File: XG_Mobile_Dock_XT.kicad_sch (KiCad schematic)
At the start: 45 parts, among them J1 5-1775443-8, J13 39301240, J14 I2C1, J2 20455-040E-76, J3 20455-040E-76, J5 USB_C_Receptacle, J6 455860005, J7 10147430-113T0LF, SW1 SW_Push

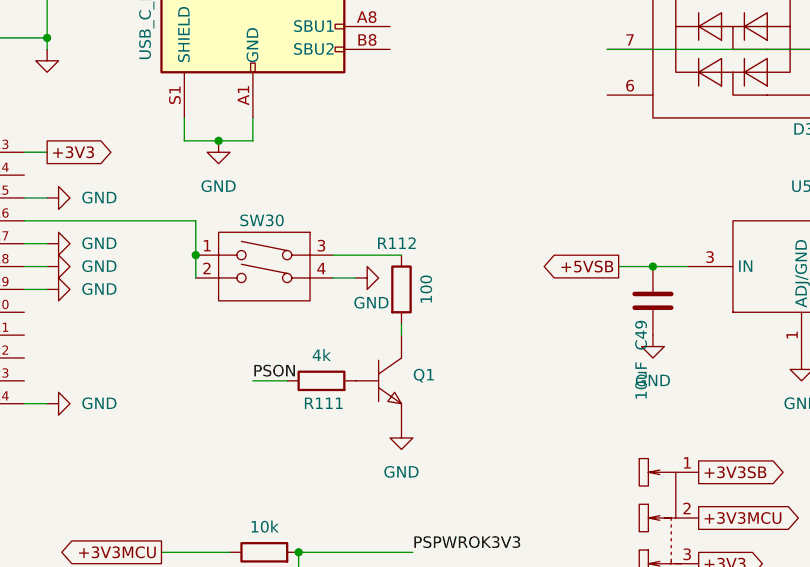
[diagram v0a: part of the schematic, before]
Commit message: connected directly transistor to ps on
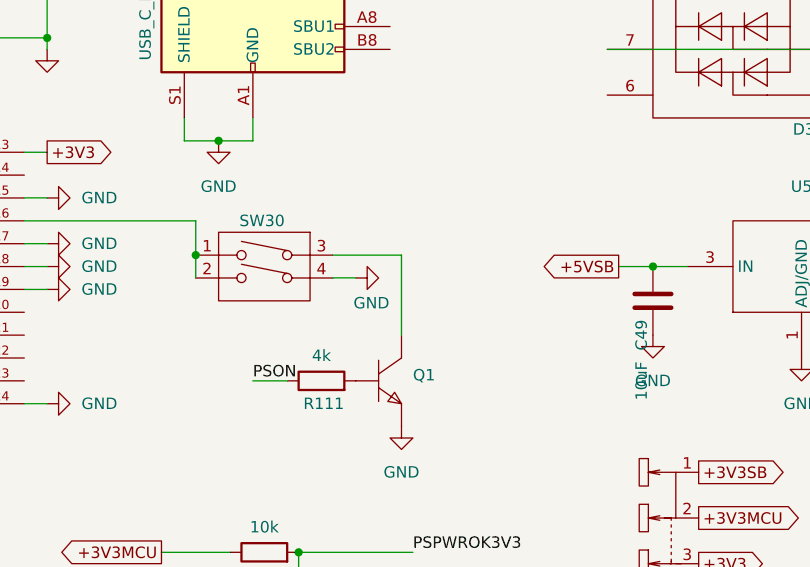
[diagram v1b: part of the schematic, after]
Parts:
- removed R112: 100, Resistor_SMD:R_0603_1608Metric, symbol Device:R
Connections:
- net at Q1.3 (C): now also SW30.3
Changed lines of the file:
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@@
 	(wire
 		(pts
-			(xy 121.92 154.94) (xy 121.92 156.21)
+			(xy 121.92 147.32) (xy 121.92 156.21)
 		)
 		(stroke
@@
 					(unit 1)
 				)
-			)
-		)
-	)
-	(symbol
-		(lib_id "Device:R")
-		(at 121.92 151.13 0)
-		(unit 1)
-		(exclude_from_sim no)
-		(in_bom yes)
-		(on_board yes)
-		(dnp no)
-		(property "Reference" "R112"
-			(at 121.412 146.05 0)
-			(effects
-				(font
-					(size 1.27 1.27)
-				)
-			)
-		)
-		(property "Value" "100"
-			(at 124.714 151.13 90)
-			(effects
-				(font
-					(size 1.27 1.27)
-				)
-			)
-		)
-		(property "Footprint" "Resistor_SMD:R_0603_1608Metric"
-			(at 120.142 151.13 90)
-			(effects
-				(font
-					(size 1.27 1.27)
-				)
-				(hide yes)
-			)
-		)
-		(property "Datasheet" "~"
-			(at 121.92 151.13 0)
-			(effects
-				(font
-					(size 1.27 1.27)
-				)
-				(hide yes)
-			)
-		)
-		(property "Description" "Resistor"
-			(at 121.92 151.13 0)
-			(effects
-				(font
-					(size 1.27 1.27)
-				)
-				(hide yes)
-			)
-		)
-		(property "LCSC" "C22775"
-			(at 121.92 151.13 0)
-			(effects
-				(font
-					(size 1.27 1.27)
-				)
-				(hide yes)
-			)
-		)
-		(property "Part_Number" "0603WAF1000T5E"
-			(at 121.92 151.13 0)
-			(effects
-				(font
-					(size 1.27 1.27)
-				)
-				(hide yes)
-			)
-		)
-		(property "Vend" ""
-			(at 121.92 151.13 0)
-			(effects
-				(font
-					(size 1.27 1.27)
-				)
-				(hide yes)
-			)
-		)
-		(property "Vendor" ""
-			(at 121.92 151.13 0)
-			(effects
-				(font
-					(size 1.27 1.27)
-				)
-				(hide yes)
-			)
-		)
-		(property "Category" ""
-			(at 121.92 151.13 0)
-			(effects
-				(font
-					(size 1.27 1.27)
-				)
-				(hide yes)
-			)
-		)
-		(property "DK_Datasheet_Link" ""
-			(at 121.92 151.13 0)
-			(effects
-				(font
-					(size 1.27 1.27)
-				)
-				(hide yes)
-			)
-		)
-		(property "DK_Detail_Page" ""
-			(at 121.92 151.13 0)
-			(effects
-				(font
-					(size 1.27 1.27)
-				)
-				(hide yes)
-			)
-		)
-		(property "Family" ""
-			(at 121.92 151.13 0)
-			(effects
-				(font
-					(size 1.27 1.27)
-				)
-				(hide yes)
-			)
-		)
-		(property "MPN" ""
-			(at 121.92 151.13 0)
-			(effects
-				(font
-					(size 1.27 1.27)
-				)
-				(hide yes)
-			)
-		)
-		(property "Manufacturer" ""
-			(at 121.92 151.13 0)
-			(effects
-				(font
-					(size 1.27 1.27)
-				)
-				(hide yes)
-			)
-		)
-		(property "Status" ""
-			(at 121.92 151.13 0)
-			(effects
-				(font
-					(size 1.27 1.27)
-				)
-				(hide yes)
-			)
-		)
-		(property "Sim.Device" ""
-			(at 121.92 151.13 0)
-			(effects
-				(font
-					(size 1.27 1.27)
-				)
-				(hide yes)
-			)
-		)
-		(property "Sim.Pins" ""
-			(at 121.92 151.13 0)
-			(effects
-				(font
-					(size 1.27 1.27)
-				)
-				(hide yes)
-			)
-		)
-		(property "Sim.Type" ""
-			(at 121.92 151.13 0)
-			(effects
-				(font
-					(size 1.27 1.27)
-				)
-				(hide yes)
-			)
-		)
-		(pin "2"
-		)
-		(pin "1"
-		)
-		(instances
-			(project "XG_Mobile_Dock_XT"
-				(path "/f97e6956-ab08-42cb-8fed-03fa58e87f0e"
-					(reference "R112")
-					(unit 1)
-				)

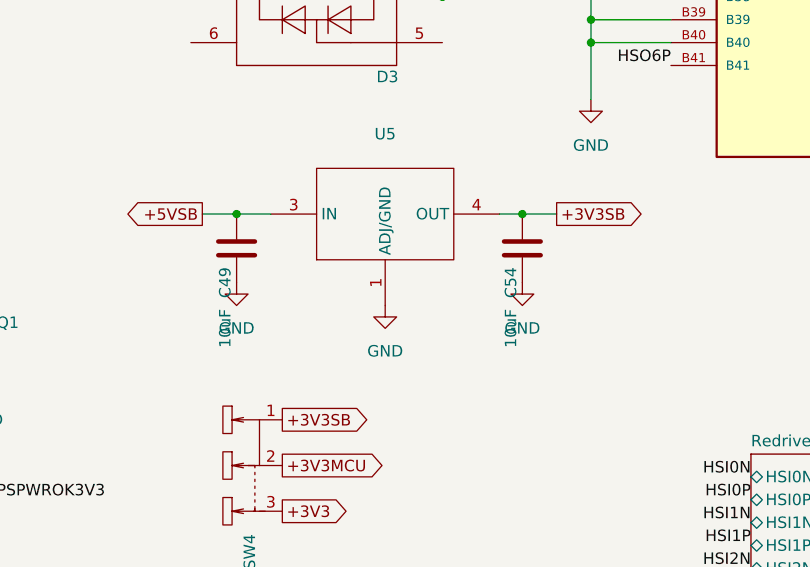
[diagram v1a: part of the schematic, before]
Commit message: added proper capacitators for ldo
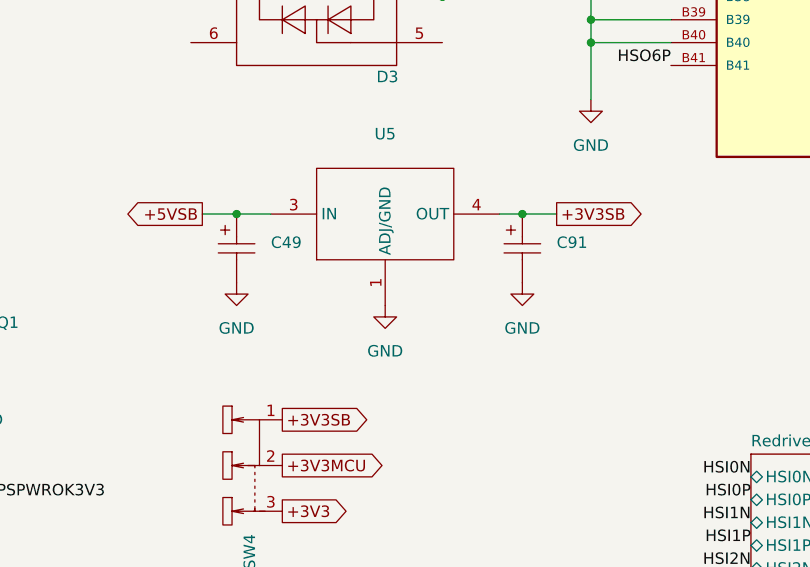
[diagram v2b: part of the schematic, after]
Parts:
- removed C49, C54: 10uF, Capacitor_SMD:C_0603_1608Metric, symbol Device:C
- added C49, C91: 10uF, TAJA106K016RNJ:CAP-SMD_L3.2-W1.6-RD-C7171, symbol TAJA106K016RNJ:TAJA106K016RNJ
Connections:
- net +3V3SB: now also C91.1
- net +5VSB: now also C49.1
- net GND: now also C49.2, C91.2
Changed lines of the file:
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@@
 	)
 	(junction
+		(at 149.86 148.59)
+		(diameter 0)
+		(color 0 0 0 0)
+	)
+	(junction
 		(at 236.22 58.42)
 		(diameter 0)
@@
 	)
 	(junction
-		(at 149.86 148.59)
-		(diameter 0)
-		(color 0 0 0 0)
-	)
-	(junction
 		(at 236.22 99.06)
 		(diameter 0)
@@
 	)
 	(junction
-		(at 181.61 148.59)
-		(diameter 0)
-		(color 0 0 0 0)
-	)
-	(junction
 		(at 82.55 115.57)
 		(diameter 0)
@@
 	)
 	(junction
+		(at 181.61 148.59)
+		(diameter 0)
+		(color 0 0 0 0)
+	)
+	(junction
 		(at 46.99 19.05)
 		(diameter 0)
@@
 	(wire
 		(pts
-			(xy 181.61 148.59) (xy 185.42 148.59)
-		)
-		(stroke
-			(width 0)
-			(type default)
-		)
-	)
-	(wire
-		(pts
 			(xy 236.22 109.22) (xy 236.22 114.3)
 		)
@@
 	(wire
 		(pts
+			(xy 181.61 148.59) (xy 185.42 148.59)
+		)
+		(stroke
+			(width 0)
+			(type default)
+		)
+	)
+	(wire
+		(pts
 			(xy 172.72 91.44) (xy 175.26 91.44)
 		)
@@
 	(wire
 		(pts
-			(xy 149.86 148.59) (xy 153.67 148.59)
+			(xy 146.05 148.59) (xy 149.86 148.59)
 		)
 		(stroke
@@
 	(wire
 		(pts
-			(xy 146.05 148.59) (xy 149.86 148.59)
-		)
-		(stroke
-			(width 0)
-			(type default)
-		)
-	)
-	(wire
-		(pts
 			(xy 123.19 22.86) (xy 129.54 22.86)
 		)
@@
 	(wire
 		(pts
+			(xy 149.86 148.59) (xy 153.67 148.59)
+		)
+		(stroke
+			(width 0)
+			(type default)
+		)
+	)
+	(wire
+		(pts
 			(xy 38.1 153.67) (xy 40.64 153.67)
 		)
@@
 	)
 	(symbol
-		(lib_id "Device:C")
-		(at 149.86 152.4 0)
-		(mirror x)
-		(unit 1)
-		(exclude_from_sim no)
-		(in_bom yes)
-		(on_board yes)
-		(dnp no)
-		(property "Reference" "C49"
-			(at 148.59 156.21 90)
-			(effects
-				(font
-					(size 1.27 1.27)
-				)
-			)
-		)
-		(property "Value" "10uF"
-			(at 148.59 161.29 90)
-			(effects
-				(font
-					(size 1.27 1.27)
-				)
-			)
-		)
-		(property "Footprint" "Capacitor_SMD:C_0603_1608Metric"
-			(at 150.8252 148.59 0)
-			(effects
-				(font
-					(size 1.27 1.27)
-				)
-				(hide yes)
-			)
-		)
-		(property "Datasheet" "~"
-			(at 149.86 152.4 0)
-			(effects
-				(font
-					(size 1.27 1.27)
-				)
-				(hide yes)
-			)
-		)
-		(property "Description" "Unpolarized capacitor"
-			(at 149.86 152.4 0)
-			(effects
-				(font
-					(size 1.27 1.27)
-				)
-				(hide yes)
-			)
-		)
-		(property "Part_Number" "CL10A106KP8NNNC"
-			(at 149.86 152.4 0)
-			(effects
-				(font
-					(size 1.27 1.27)
-				)
-				(hide yes)
-			)
-		)
-		(property "LCSC" "C19702"
-			(at 149.86 152.4 0)
-			(effects
-				(font
-					(size 1.27 1.27)
-				)
-				(hide yes)
-			)
-		)
-		(pin "1"
-		)
-		(pin "2"
-		)
-		(instances
-			(project "XG_Mobile_Dock_XT"
-				(path "/f97e6956-ab08-42cb-8fed-03fa58e87f0e"
-					(reference "C49")
-					(unit 1)
-				)
-			)
-		)
-	)
-	(symbol
 		(lib_id "power:PWR_FLAG")
 		(at 189.23 24.13 0)
@@
 	)
 	(symbol
-		(lib_id "Device:C")
-		(at 181.61 152.4 0)
-		(mirror x)
-		(unit 1)
-		(exclude_from_sim no)
-		(in_bom yes)
-		(on_board yes)
-		(dnp no)
-		(property "Reference" "C54"
-			(at 180.34 156.21 90)
-			(effects
-				(font
-					(size 1.27 1.27)
-				)
-			)
-		)
-		(property "Value" "10uF"
-			(at 180.34 161.29 90)
-			(effects
-				(font
-					(size 1.27 1.27)
-				)
-			)
-		)
-		(property "Footprint" "Capacitor_SMD:C_0603_1608Metric"
-			(at 182.5752 148.59 0)
-			(effects
-				(font
-					(size 1.27 1.27)
-				)
-				(hide yes)
-			)
-		)
-		(property "Datasheet" "~"
-			(at 181.61 152.4 0)
-			(effects
-				(font
-					(size 1.27 1.27)
-				)
-				(hide yes)
-			)
-		)
-		(property "Description" "Unpolarized capacitor"
-			(at 181.61 152.4 0)
-			(effects
-				(font
-					(size 1.27 1.27)
-				)
-				(hide yes)
-			)
-		)
-		(property "Part_Number" "CL10A106KP8NNNC"
-			(at 181.61 152.4 0)
-			(effects
-				(font
-					(size 1.27 1.27)
-				)
-				(hide yes)
-			)
-		)
-		(property "LCSC" "C19702"
-			(at 181.61 152.4 0)
-			(effects
-				(font
-					(size 1.27 1.27)
-				)
-				(hide yes)
-			)
-		)
-		(pin "1"
-		)
-		(pin "2"
-		)
-		(instances
-			(project "XG_Mobile_Dock_XT"
-				(path "/f97e6956-ab08-42cb-8fed-03fa58e87f0e"
-					(reference "C54")
-					(unit 1)
-				)
-			)
-		)
-	)
-	(symbol
 		(lib_id "Device:R")
 		(at 92.71 191.77 90)
@@
 	)
 	(symbol
+		(lib_id "TAJA106K016RNJ:TAJA106K016RNJ")
+		(at 181.61 152.4 90)
+		(unit 1)
+		(exclude_from_sim no)
+		(in_bom yes)
+		(on_board yes)
+		(dnp no)
+		(fields_autoplaced yes)
+		(property "Reference" "C91"
+			(at 185.42 151.7649 90)
+			(effects
+				(font
+					(size 1.27 1.27)
+				)
+				(justify right)
+			)
+		)
+		(property "Value" "10uF"
+			(at 181.61 152.4 0)
+			(effects
+				(font
+					(size 1.27 1.27)
+				)
+				(hide yes)
+			)
+		)
+		(property "Footprint" "TAJA106K016RNJ:CAP-SMD_L3.2-W1.6-RD-C7171"
+			(at 181.61 152.4 0)
+			(effects
+				(font
+					(size 1.27 1.27)
+				)
+				(hide yes)
+			)
+		)
+		(property "Datasheet" ""
+			(at 181.61 152.4 0)
+			(effects
+				(font
+					(size 1.27 1.27)
+				)
+				(hide yes)
+			)
+		)
+		(property "Description" "Capacitance:10uF Tolerance:±10% Tolerance:±10% Voltage Rating:16V Equivalent Series Resistance(ESR):3Ω@100kHz Operating Temperature:-55°C~+125°C Operating Temperature:-55°C~+125°C"
+			(at 181.61 152.4 0)
+			(effects
+				(font
+					(size 1.27 1.27)
+				)
+				(hide yes)
+			)
+		)
+		(property "Part_Number" "TAJA106K016RNJ"
+			(at 181.61 152.4 0)
+			(effects
+				(font
+					(size 1.27 1.27)
+				)
+				(hide yes)
+			)
+		)
+		(property "Manufacturer" "Kyocera AVX"
+			(at 181.61 152.4 0)
+			(effects
+				(font
+					(size 1.27 1.27)
+				)
+				(hide yes)
+			)
+		)
+		(property "LCSC" "C7171"
+			(at 181.61 152.4 0)
+			(effects
+				(font
+					(size 1.27 1.27)
+				)
+				(hide yes)
+			)
+		)
+		(pin "1"
+		)
+		(pin "2"
+		)
+		(instances
+			(project ""
+				(path "/f97e6956-ab08-42cb-8fed-03fa58e87f0e"
+					(reference "C91")
+					(unit 1)
+				)
+			)
+		)
+	)
+	(symbol
 		(lib_id "power:+3V3")
 		(at 387.35 86.36 0)
@@
 					(unit 1)
 				)
+			)
+		)
+	)
+	(symbol
+		(lib_id "TAJA106K016RNJ:TAJA106K016RNJ")
+		(at 149.86 152.4 90)
+		(unit 1)
+		(exclude_from_sim no)
+		(in_bom yes)
+		(on_board yes)
+		(dnp no)
+		(fields_autoplaced yes)
+		(property "Reference" "C49"
+			(at 153.67 151.7649 90)
+			(effects
+				(font
+					(size 1.27 1.27)
+				)
+				(justify right)
+			)
+		)
+		(property "Value" "10uF"
+			(at 149.86 152.4 0)
+			(effects
+				(font
+					(size 1.27 1.27)
+				)
+				(hide yes)
+			)
+		)
+		(property "Footprint" "TAJA106K016RNJ:CAP-SMD_L3.2-W1.6-RD-C7171"
+			(at 149.86 152.4 0)
+			(effects
+				(font
+					(size 1.27 1.27)
+				)
+				(hide yes)
+			)
+		)
+		(property "Datasheet" ""
+			(at 149.86 152.4 0)
+			(effects
+				(font
+					(size 1.27 1.27)
+				)
+				(hide yes)
+			)
+		)
+		(property "Description" "Capacitance:10uF Tolerance:±10% Tolerance:±10% Voltage Rating:16V Equivalent Series Resistance(ESR):3Ω@100kHz Operating Temperature:-55°C~+125°C Operating Temperature:-55°C~+125°C"
+			(at 149.86 152.4 0)
+			(effects
+				(font
+					(size 1.27 1.27)
+				)
+				(hide yes)
+			)
+		)
+		(property "Part_Number" "TAJA106K016RNJ"
+			(at 149.86 152.4 0)
+			(effects
+				(font
+					(size 1.27 1.27)
+				)
+				(hide yes)
+			)
+		)
+		(property "Manufacturer" "Kyocera AVX"
+			(at 149.86 152.4 0)
+			(effects
+				(font
+					(size 1.27 1.27)
+				)
+				(hide yes)
+			)
+		)
+		(property "LCSC" "C7171"
+			(at 149.86 152.4 0)
+			(effects
+				(font
+					(size 1.27 1.27)
+				)
+				(hide yes)
+			)
+		)
+		(pin "1"
+		)
+		(pin "2"
+		)
+		(instances
+			(project "XG_Mobile_Dock_XT"
+				(path "/f97e6956-ab08-42cb-8fed-03fa58e87f0e"
+					(reference "C49")
+					(unit 1)
+				)

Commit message: fixs
final fixes
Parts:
- Q1, Q2: LCSC (none) -> C2145; LCSC Part Name hfe=200~300 -> (none); Manufacturer CJ(江苏长电/长晶) -> (none); Manufacturer Part MMBT5551(RANGE:200-300) -> (none); Part_Number (none) -> MMBT5551(RANGE:200-300); Supplier LCSC -> (none); Supplier Part C2145 -> (none)
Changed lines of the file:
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@@
 			)
 		)
-		(property "Manufacturer Part" "MMBT5551(RANGE:200-300)"
+		(property "Part_Number" "MMBT5551(RANGE:200-300)"
 			(at 119.38 161.29 0)
 			(effects
@@
 			)
 		)
-		(property "Manufacturer" "CJ(江苏长电/长晶)"
-			(at 119.38 161.29 0)
-			(effects
-				(font
-					(size 1.27 1.27)
-				)
-				(hide yes)
-			)
-		)
-		(property "Supplier Part" "C2145"
-			(at 119.38 161.29 0)
-			(effects
-				(font
-					(size 1.27 1.27)
-				)
-				(hide yes)
-			)
-		)
-		(property "Supplier" "LCSC"
-			(at 119.38 161.29 0)
-			(effects
-				(font
-					(size 1.27 1.27)
-				)
-				(hide yes)
-			)
-		)
-		(property "LCSC Part Name" "hfe=200~300"
+		(property "LCSC" "C2145"
 			(at 119.38 161.29 0)
 			(effects
@@
 			)
 		)
-		(property "Manufacturer Part" "MMBT5551(RANGE:200-300)"
+		(property "Part_Number" "MMBT5551(RANGE:200-300)"
 			(at 107.95 191.77 0)
 			(effects
@@
 			)
 		)
-		(property "Manufacturer" "CJ(江苏长电/长晶)"
+		(property "LCSC" "C2145"
 			(at 107.95 191.77 0)
 			(effects
-				(font
-					(size 1.27 1.27)
-				)
-				(hide yes)
-			)
-		)
-		(property "Supplier Part" "C2145"
-			(at 107.95 191.77 0)
-			(effects
-				(font
-					(size 1.27 1.27)
-				)
-				(hide yes)
-			)
-		)
-		(property "Supplier" "LCSC"
-			(at 107.95 191.77 0)
-			(effects
-				(font
-					(size 1.27 1.27)
-				)
-				(hide yes)
-			)
-		)
-		(property "LCSC Part Name" "hfe=200~300"
-			(at 107.95 191.77 0)
-			(effects

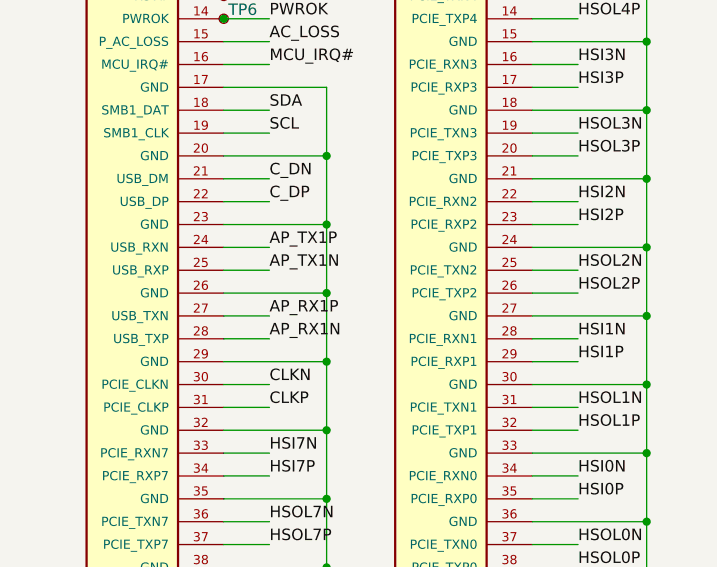
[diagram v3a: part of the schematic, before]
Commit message: usb rimter polarity
same polarity for usb retimer
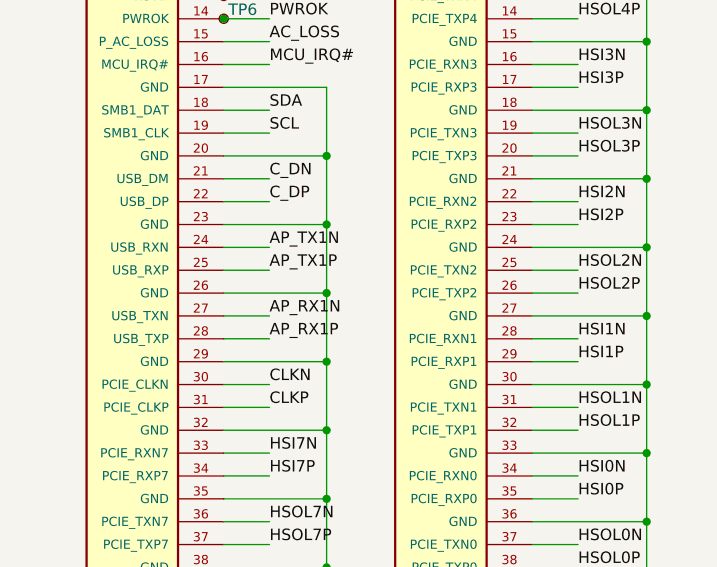
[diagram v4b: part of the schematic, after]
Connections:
- net AP_RX1N: now also J3.27 (USB_TXN); no longer J3.28 (USB_TXP)
- net AP_RX1P: now also J3.28 (USB_TXP); no longer J3.27 (USB_TXN)
- net AP_TX1N: now also J3.24 (USB_RXN); no longer J3.25 (USB_RXP)
- net AP_TX1P: now also J3.25 (USB_RXP); no longer J3.24 (USB_RXN)
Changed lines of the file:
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@@
 	)
 	(label "AP_RX1P"
-		(at 40.64 85.09 0)
+		(at 40.64 87.63 0)
 		(effects
 			(font
@@
 	)
 	(label "AP_TX1P"
-		(at 40.64 77.47 0)
+		(at 40.64 80.01 0)
 		(effects
 			(font
@@
 	)
 	(label "AP_TX1N"
-		(at 40.64 80.01 0)
+		(at 40.64 77.47 0)
 		(effects
 			(font
@@
 	)
 	(label "AP_RX1N"
-		(at 40.64 87.63 0)
-		(effects
-			(font
+		(at 40.64 85.09 0)
+		(effects
+			(font
